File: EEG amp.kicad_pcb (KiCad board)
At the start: 2 copper layers, 39 parts, among them J1 Electrodes, J2 Power, J3 Output, J4 Status, U1 AD8232, U2 TMUX154EDGS

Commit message: Designed PCB and apparently did something to the schematic
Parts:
- added D4: Red, LED_THT:LED_D5.0mm, F.Cu at (148.8, 104.8)
- moved R1 41.3 mm to (158.5, 82.0), turned to -90 degrees
- moved R2 41.3 mm to (158.5, 84.0), turned to -90 degrees
- moved C2 37.6 mm to (161.5, 82.5)
- moved C3 34.2 mm to (141.4, 89.4), turned to -90 degrees
- moved C4 30.2 mm to (146.0, 83.5), turned to 90 degrees
- moved R16 29.6 mm to (140.5, 92.0), turned to -90 degrees
- moved R19 27.8 mm to (155.0, 99.1)
- moved R9 26.1 mm to (136.6, 117.4), turned to 180 degrees
- moved C8 25.3 mm to (146.7, 92.3), turned to -90 degrees
- moved C7 25.0 mm to (147.0, 91.0)
- moved R8 19.5 mm to (141.6, 117.4), turned to 180 degrees
- moved R17 18.8 mm to (140.5, 94.5), turned to -90 degrees
- moved R15 16.8 mm to (140.1, 104.4)
- moved R12 15.3 mm to (144.0, 107.9)
- moved R6 15.3 mm to (138.4, 107.8)
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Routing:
- net GND: track 40.7 -> 127.8 mm, vias 0 -> 7
- net connected1: track 0.00 -> 85.4 mm, vias 0 -> 2
- net Net-(C5-Pad1): track 0.00 -> 71.4 mm
- net IAOUT1: track 2.54 -> 71.0 mm, vias 0 -> 2
- net 1o: track 0.00 -> 57.2 mm, vias 0 -> 1
- net +3.3V: track 54.5 -> 106.2 mm
- net Net-(U1-OUT): track 0.00 -> 44.4 mm, vias 0 -> 2
- net OPAMP+1: track 0.00 -> 44.0 mm, vias 0 -> 2
- net +5V: track 1.48 -> 45.3 mm, vias 0 -> 4
- net REFOUT1: track 0.00 -> 33.1 mm, vias 0 -> 2
- net shutdown: track 17.3 -> 49.1 mm, vias 0 -> 1
- net Ie: track 47.2 -> 15.8 mm, vias 0 -> 2
- net Ge: track 0.00 -> 23.8 mm, vias 0 -> 1
- net OPAMP-1: track 0.00 -> 23.0 mm
- net RLD1: track 0.00 -> 14.4 mm, vias 0 -> 2
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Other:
- board outline added: 53 x 42.2 mm
- board text added: "5V 3.3V GND"
- board text added: "Conn Shtdn Swtch"
- board text added: "Connected"
- board text added: "Electrode 1"
- board text added: "Electrode 2"
- board text added: "GE 1E ZE 2E"
- board text added: "On"
- board text added: "Out"

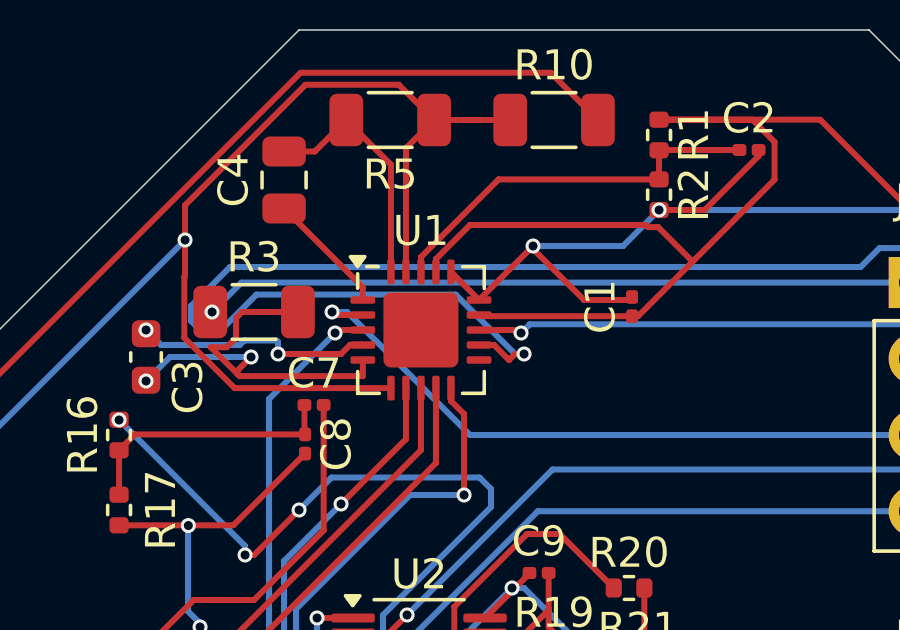
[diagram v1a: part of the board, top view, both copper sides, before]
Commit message: Changed gitignore, reorganized schematic a bit, connected EP to ground, and updated the symbol
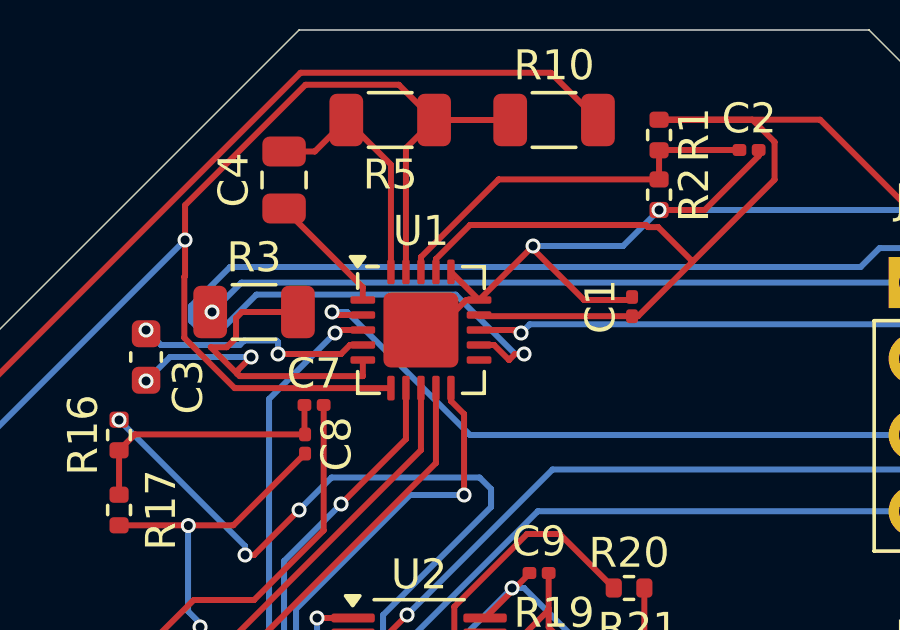
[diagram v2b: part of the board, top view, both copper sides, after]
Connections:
- net Net-(U1-OUT) renamed UFOUT1
- U1 pad 21: (no net) -> GND
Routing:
- net GND: track 127.8 -> 130.2 mm
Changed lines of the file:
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@@
 	(net 9 "1o")
 	(net 10 "REFOUT1")
-	(net 11 "Net-(U1-OUT)")
+	(net 11 "UFOUT1")
 	(net 12 "Aref")
 	(net 13 "+5V")
@@
 	(net 30 "Net-(U2-B0)")
 	(net 31 "Net-(U2-B)")
-	(net 32 "unconnected-(U1-LOD--Pad11)")
-	(net 33 "Ie")
+	(net 32 "Ie")
+	(net 33 "unconnected-(U1-LOD--Pad11)")
 	(footprint "Resistor_SMD:R_0402_1005Metric"
 		(layer "F.Cu")
@@
 			(layers "F.Cu" "F.Paste" "F.Mask")
 			(roundrect_rratio 0.25)
-			(net 11 "Net-(U1-OUT)")
+			(net 11 "UFOUT1")
 			(pintype "passive")
 		)
@@
 			(layers "F.Cu" "F.Paste" "F.Mask")
 			(roundrect_rratio 0.25)
-			(net 33 "Ie")
+			(net 32 "Ie")
 			(pinfunction "A")
 			(pintype "passive")
@@
 			(layers "F.Cu" "F.Paste" "F.Mask")
 			(roundrect_rratio 0.25)
-			(net 33 "Ie")
+			(net 32 "Ie")
 			(pinfunction "~{IN}")
 			(pintype "input")
@@
 			(layers "F.Cu" "F.Paste" "F.Mask")
 			(roundrect_rratio 0.25)
-			(net 11 "Net-(U1-OUT)")
+			(net 11 "UFOUT1")
 			(pinfunction "OUT")
 			(pintype "output")
@@
 			(layers "F.Cu" "F.Paste" "F.Mask")
 			(roundrect_rratio 0.25)
-			(net 32 "unconnected-(U1-LOD--Pad11)")
+			(net 33 "unconnected-(U1-LOD--Pad11)")
 			(pinfunction "LOD-")
 			(pintype "output+no_connect")
@@
 			(layers "F.Cu" "F.Mask")
 			(roundrect_rratio 0.1)
+			(net 1 "GND")
+			(pinfunction "EP")
+			(pintype "passive")
 		)
 		(model "${KICAD8_3DMODEL_DIR}/Package_CSP.3dshapes/LFCSP-20-1EP_4x4mm_P0.5mm_EP2.5x2.5mm.wrl"
@@
 			(layers "F.Cu" "F.Mask")
 			(roundrect_rratio 0.25)
-			(net 11 "Net-(U1-OUT)")
+			(net 11 "UFOUT1")
 			(pintype "passive")
 		)
@@
 	)
 	(segment
+		(start 151.073114 88.5)
+		(end 152.073114 87.5)
+		(width 0.2)
+		(layer "F.Cu")
+		(net 1)
+	)
+	(segment
 		(start 157.39 98.98)
 		(end 158.01 99.6)
@@
 	)
 	(segment
+		(start 152.073114 87.5)
+		(end 152.5 87.5)
+		(width 0.2)
+		(layer "F.Cu")
+		(net 1)
+	)
+	(segment
 		(start 158.01 97.1)
 		(end 158.01 99.6)
@@
 		(net 1)
 	)
+	(segment
+		(start 150.5625 88.5)
+		(end 151.073114 88.5)
+		(width 0.2)
+		(layer "F.Cu")
+		(net 1)
+	)
 	(via
 		(at 154.3 85.7)
@@
 		(width 0.2)
 		(layer "F.Cu")
-		(net 33)
+		(net 32)
 	)
 	(segment
@@
 		(width 0.2)
 		(layer "F.Cu")
-		(net 33)
+		(net 32)
 	)
 	(segment
@@
 		(width 0.2)
 		(layer "F.Cu")
-		(net 33)
+		(net 32)
 	)
 	(segment
@@
 		(width 0.2)
 		(layer "F.Cu")
-		(net 33)
+		(net 32)
 	)
 	(segment
@@
 		(width 0.2)
 		(layer "F.Cu")
-		(net 33)
+		(net 32)
 	)
 	(via
@@
 		(drill 0.3)
 		(layers "F.Cu" "B.Cu")
-		(net 33)
+		(net 32)
 	)
 	(via
@@
 		(drill 0.3)
 		(layers "F.Cu" "B.Cu")
-		(net 33)
+		(net 32)
 	)
 	(segment
@@
 		(width 0.2)
 		(layer "B.Cu")
-		(net 33)
+		(net 32)
 	)
 	(segment
@@
 		(width 0.2)
 		(layer "B.Cu")
-		(net 33)
+		(net 32)
 	)
 	(segment
@@
 		(width 0.2)
 		(layer "B.Cu")
-		(net 33)
+		(net 32)
 	)
 )

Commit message: Messed with schematic and(I think) finished PCB
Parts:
- removed C9: 100nF, Capacitor_SMD:C_0201_0603Metric
- removed R11, R12: 33k, Resistor_SMD:R_1206_3216Metric
- removed R16, R17: 10k ±0.1%, Resistor_SMD:R_0402_1005Metric
- removed R19, R20, R21: 50R, Resistor_SMD:R_0402_1005Metric
- removed R9: 150, Resistor_SMD:R_1206_3216Metric
- C1, C2, C8: value 0.1uF -> ECHU1C104GX5; footprint Capacitor_SMD:C_0201_0603Metric -> Capacitor_SMD:C_1210_3225Metric
- C3: value 1nF -> CC0402JRX7R9BB102; footprint Capacitor_SMD:C_0603_1608Metric -> Capacitor_SMD:C_0402_1005Metric
- C4: value 100uF -> CA45-B6R3K107T; footprint Capacitor_SMD:C_0805_2012Metric -> Capacitor_Tantalum_SMD:CP_EIA-3528-21_Kemet-B
- C5, C6: value 10uF -> CA45-A010K106T; footprint Capacitor_SMD:C_0805_2012Metric -> Capacitor_Tantalum_SMD:CP_EIA-3216-12_Kemet-S
- C7: value 14pF -> 0402CG140J500NT; footprint Capacitor_SMD:C_0201_0603Metric -> Capacitor_SMD:C_0402_1005Metric
- D1: value Green -> XL-1608UBC-04; footprint LED_THT:LED_D5.0mm -> LED_SMD:LED_0603_1608Metric
- D2: value Yellow - 2e -> XL-1608UGC-04; footprint LED_THT:LED_D5.0mm -> LED_SMD:LED_0603_1608Metric
- D3: value Yellow - 1e -> XL-1608UGC-04; footprint LED_THT:LED_D5.0mm -> LED_SMD:LED_0603_1608Metric
- D4: value Red -> XL-2012UWC; footprint LED_THT:LED_D5.0mm -> LED_SMD:LED_0805_2012Metric
- J2: footprint Connector_PinSocket_2.54mm:PinSocket_1x03_P2.54mm_Vertical -> Connector_PinSocket_2.54mm:PinSocket_1x04_P2.54mm_Vertical
- R1, R2: value 10k ±0.1% -> ARG03BTC1002; footprint Resistor_SMD:R_0402_1005Metric -> Resistor_SMD:R_0603_1608Metric
- R10: value 33k -> 0603WAD3302T5E; footprint Resistor_SMD:R_1206_3216Metric -> Resistor_SMD:R_0603_1608Metric
- R13: value 1k -> CF1/6W-7.5KΩ±5%T52; footprint Resistor_SMD:R_1206_3216Metric -> Resistor_THT:R_Axial_DIN0207_L6.3mm_D2.5mm_P5.08mm_Vertical
- R14, R15, R18: value 10k -> 1206W4F1002T5E; footprint Resistor_SMD:R_0402_1005Metric -> Resistor_SMD:R_1206_3216Metric
- R3, R5: value 330k -> SCR0402J330K; footprint Resistor_SMD:R_1206_3216Metric -> Resistor_SMD:R_0402_1005Metric
- R4, R8: value 10 -> ARG05DTC1600; footprint Resistor_SMD:R_1206_3216Metric -> Resistor_SMD:R_0805_2012Metric
- R6: value 150 -> 0603WAD3302T5E; footprint Resistor_SMD:R_1206_3216Metric -> Resistor_SMD:R_0603_1608Metric
- R7: value 33k -> 1206W4F1002T5E
- U2: value TMUX154EDGS -> TS5A3159ADBVR; footprint Package_SO:VSSOP-10_3x3mm_P0.5mm -> Package_TO_SOT_SMD:SOT-23-6
- moved R7 34.5 mm to (170.2, 112.2), turned to 90 degrees
- moved J3 25.2 mm to (175.8, 89.9)
- moved R8 23.4 mm to (142.6, 94.0)
- moved R18 18.4 mm to (156.8, 96.6), turned to -90 degrees
- moved C8 16.5 mm to (155.2, 106.5), turned to 180 degrees
- moved R15 14.2 mm to (152.8, 98.0)
- moved R13 13.0 mm to (150.8, 105.7), turned to 90 degrees
- moved C6 12.9 mm to (146.2, 105.8)
- moved D2 11.9 mm to (159.8, 118.4), turned to 180 degrees
- moved R4 11.0 mm to (142.6, 102.2)
- moved C5 10.8 mm to (140.6, 107.2)
- moved R14 10.6 mm to (172.8, 112.2), turned to -90 degrees
- moved R6 9.97 mm to (142.6, 98.8)
- moved D3 9.97 mm to (150.0, 118.4), turned to 180 degrees
- moved C7 9.66 mm to (156.6, 92.0), turned to 180 degrees
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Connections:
- C8 pad 1: Aref -> +3.3V
- D1 pad 1: GND -> shutdown
- D1 pad 2: shutdown -> +3.3V
- D4 pad 1: connected1 -> GND
- D4 pad 2: +3.3V -> connected1
- J2 pad 1: +5V -> unconnected-(J2-Pin_1-Pad1)
- J2 pad 3: GND -> Aref
- R13 pad 2: Net-(R11-Pad2) -> OPAMP-1
- R14 pad 1: +3.3V -> shutdown
- R14 pad 2: shutdown -> +3.3V
- R15 pad 1: 1o -> OPAMP-1
- R15 pad 2: OPAMP-1 -> 1o
- R4 pad 2: Net-(R4-Pad2) -> OPAMP+1
- R6 pad 1: Net-(R4-Pad2) -> Net-(C5-Pad1)
- R7 pad 1: Net-(C5-Pad1) -> GND
- R7 pad 2: OPAMP+1 -> switch
- R8 pad 2: Net-(R8-Pad2) -> Net-(C5-Pad1)
- U2 pad 1: switch -> 2e
- U2 pad 2: 1e -> GND
- U2 pad 3: 2e -> 1e
- U2 pad 5: GND -> +3.3V
- U2 pad 6: Net-(U2-B) -> switch
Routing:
- net GND: track 130.2 -> 50.0 mm, vias 7 -> 4
- net shutdown: track 49.1 -> 99.5 mm
- net +5V: track 45.3 -> 0.00 mm, vias 4 -> 0
- net UFOUT1: track 44.4 -> 5.04 mm, vias 2 -> 0
- net IAOUT1: track 71.0 -> 36.9 mm, vias 2 -> 3
- net Net-(C5-Pad1): track 71.4 -> 43.0 mm, vias 0 -> 2
- net Ge: track 23.8 -> 50.2 mm, vias 1 -> 0
- net OPAMP+1: track 44.0 -> 18.7 mm
- net connected1: track 85.4 -> 106.1 mm, vias 2 -> 0
- net Ie: track 15.8 -> 27.1 mm
- net Net-(R11-Pad2): track 11.2 -> 0.00 mm
- net OPAMP-1: track 23.0 -> 11.9 mm, vias 0 -> 2
- net 1o: track 57.2 -> 46.4 mm, vias 1 -> 0
- net +3.3V: track 106.2 -> 96.2 mm, vias 0 -> 3
- net Aref: track 8.89 -> 18.7 mm, vias 0 -> 1
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- added copper zone on B.Cu, net GND
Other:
- board size 53 x 42.2 mm -> 47.8 x 48.2 mm
- board text added: "1E"
- board text added: "2E"
- board text added: "3.3V"
- board text added: "Aref"
- board text added: "Conn"
- board text added: "Electrodes"
- board text added: "GE"
- board text added: "GND"
- board text added: "Selected:"
- board text added: "Shtdn"
- board text added: "Switch"
- board text added: "ZE"
- board text removed: "5V 3.3V GND"
- board text removed: "Conn Shtdn Swtch"
- board text removed: "GE 1E ZE 2E"

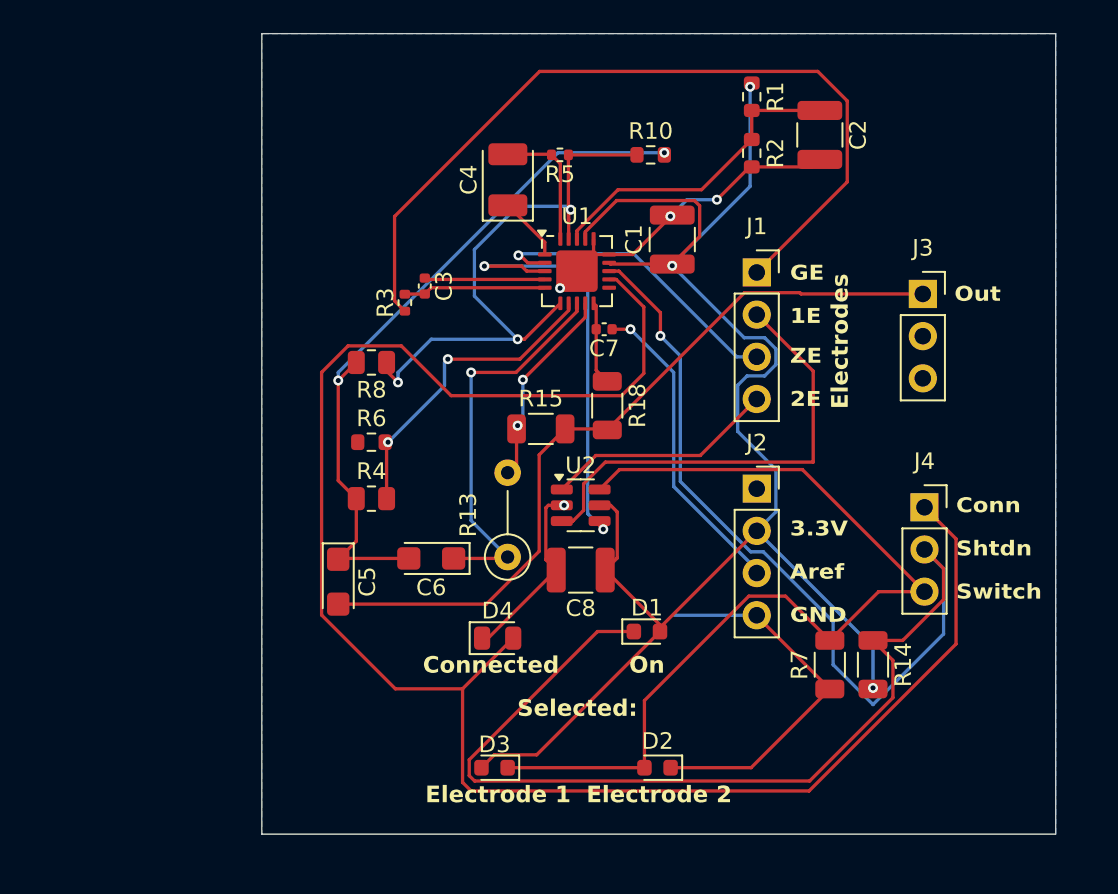
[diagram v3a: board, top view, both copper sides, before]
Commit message: Ran DRC and changed ground plane
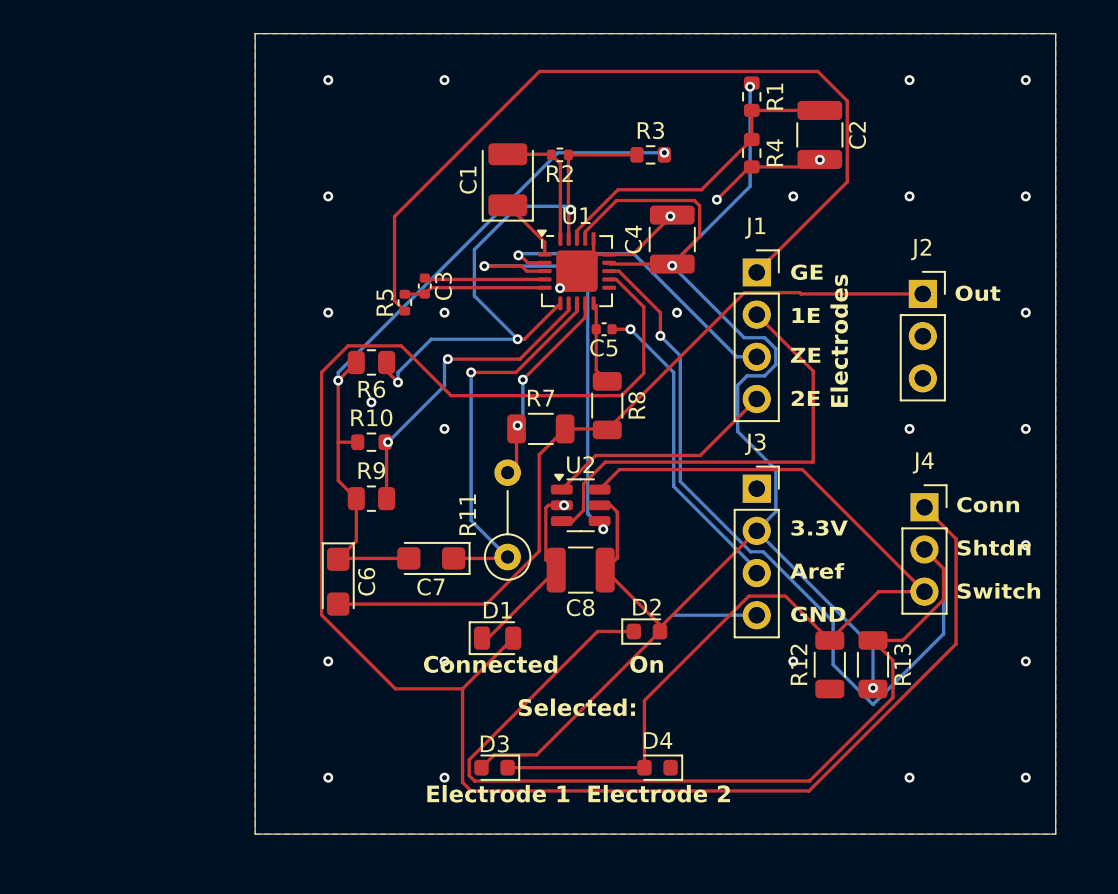
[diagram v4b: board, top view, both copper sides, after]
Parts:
- renumbered C4 to C1, C1 to C4, C7 to C5, C5 to C6, C6 to C7, D4 to D1, D1 to D2, D2 to D4, J3 to J2, J2 to J3, R6 to R10, R13 to R11, R7 to R12, R14 to R13, R5 to R2, R10 to R3, R2 to R4, R3 to R5, R8 to R6, R15 to R7, R18 to R8, R4 to R9
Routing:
- net GND: track 50.0 -> 29.6 mm, vias 4 -> 30
- net Net-(C6-Pad1): track 43.0 -> 44.2 mm
- net IAOUT1: track 36.9 -> 36.4 mm
- added copper zone on F.Cu, net GND
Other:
- board size 47.8 x 48.2 mm -> 48.2 x 48.2 mm
- board text added: "{ "ViaStitching": "0.2", "Ground plane": { "HSpacing": "7", "VSpacing": "7", "Clearance": "0", "Randomize": false } }"

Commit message: adjusted many things, including, apparently, the footprint for one of the resistors
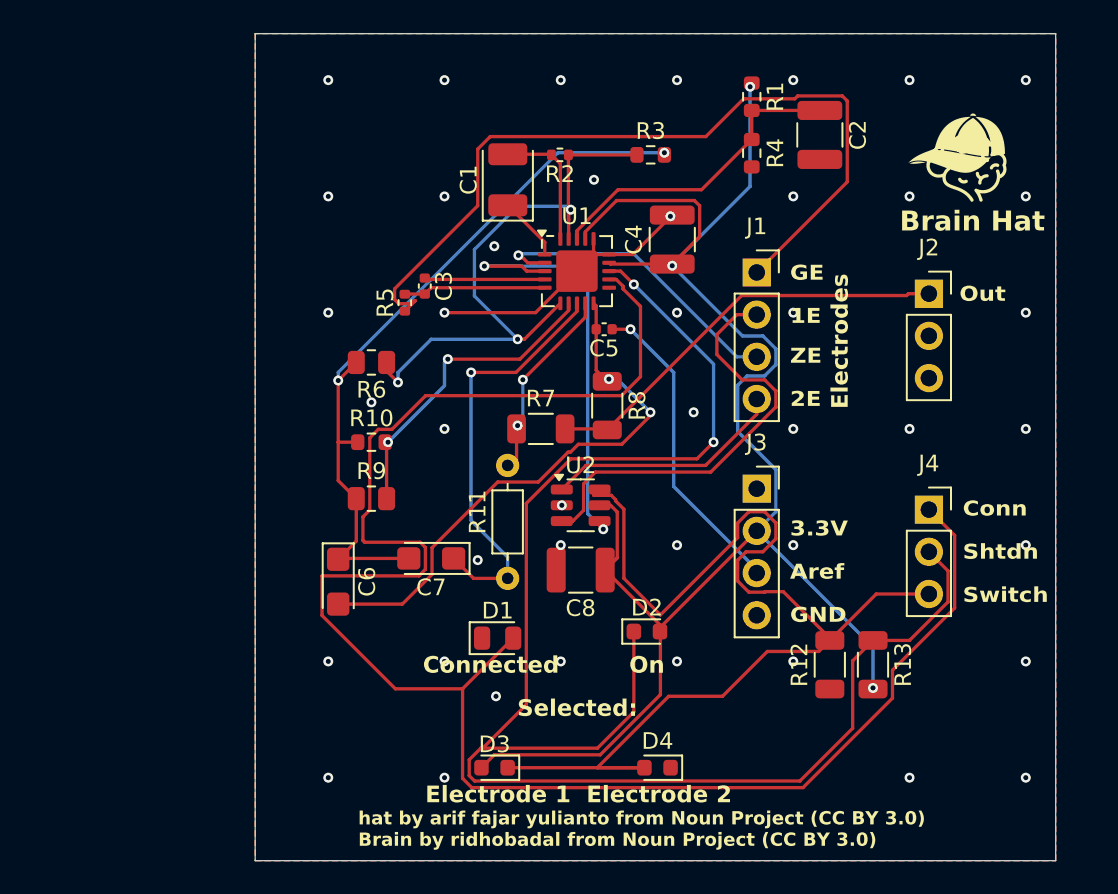
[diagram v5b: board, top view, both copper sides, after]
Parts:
- R11: footprint Resistor_THT:R_Axial_DIN0207_L6.3mm_D2.5mm_P5.08mm_Vertical -> Personal:R_Axial_DIN0207_L6.3mm_D2.5mm_P5.08mm_Horizontal
- moved R11 1.28 mm to (150.8, 107.0)
- moved J2 0.37 mm to (176.2, 89.9)
- moved J4 0.30 mm to (176.2, 102.9)
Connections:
- C6 pad 2: 1o -> UFOUT1
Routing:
- net UFOUT1: track 5.04 -> 33.0 mm, vias 0 -> 2
- net 1o: track 46.4 -> 25.2 mm
- net GND: track 29.6 -> 14.2 mm, vias 30 -> 43
- net switch: track 57.2 -> 67.9 mm
- net +3.3V: track 96.2 -> 98.4 mm
- net REFOUT1: track 23.6 -> 25.4 mm
- net 1e: track 27.8 -> 26.2 mm
- net shutdown: track 99.5 -> 98.1 mm, vias 1 -> 2
- net connected1: track 106.1 -> 107.0 mm
- net OPAMP-1: track 11.9 -> 11.1 mm
- net 2e: track 14.0 -> 14.5 mm
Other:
- board size 48.2 x 48.2 mm -> 48.2 x 49.8 mm
- board text added: "Brain Hat"
- board text added: "hat by arif fajar yulianto from Noun Project (CC BY 3.0) Brain by ridhobadal from Noun Project (CC BY 3.0)"
